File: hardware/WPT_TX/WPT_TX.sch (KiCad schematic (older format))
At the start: 121 parts, among them J1 Conn_01x01, J10 Conn_01x01, J2 Conn_01x01, J3 Conn_Coaxial, J4 Conn_Coaxial, J5 Conn_Coaxial, J6 Conn_02x05_Odd_Even, J7 Conn_01x03, J8 Conn_01x04, J9 Conn_01x01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

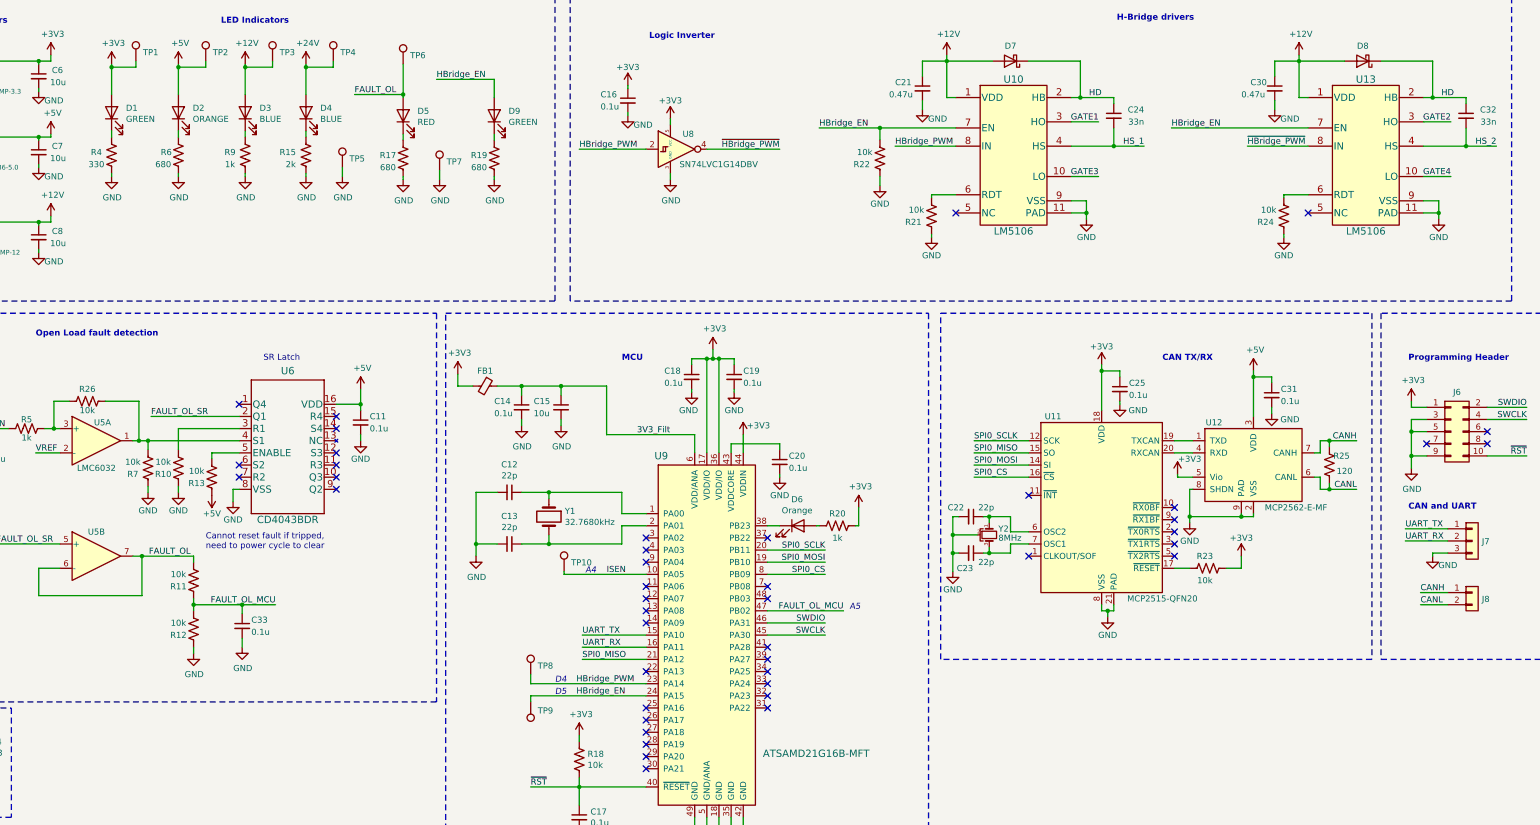
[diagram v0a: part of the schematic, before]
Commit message: Schematic Updates
- Removed "HD" net label from HB pins on gate drivers. This resulted in a critical failure on the original board and was fixed with a bodge.
- Added an extra voltage divider to ISEN input to reduce chance of 5V overvolt scenario.
- Increased series resistor value for blue LEDs by a factor of 2. Waaaay too bright.
- Decreased series resistor for 3V3 LED indicator, too dim.
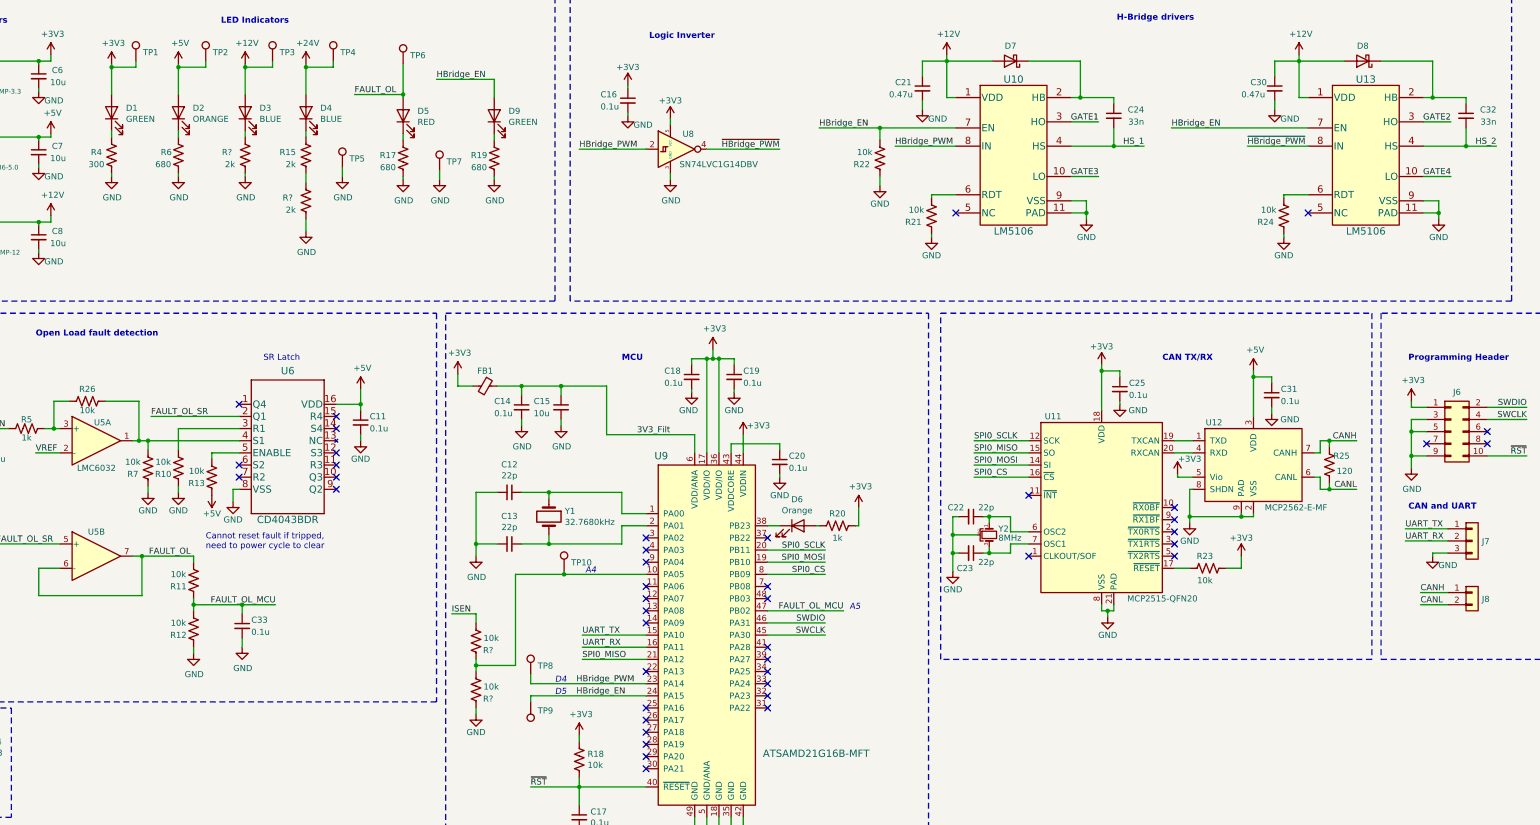
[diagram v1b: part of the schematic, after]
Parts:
- removed R9: 1k, Resistor_SMD:R_0603_1608Metric, symbol WPT_TX-rescue:R_US-Device
- added R? (x2): 10k, Resistor_SMD:R_0603_1608Metric, symbol WPT_TX-rescue:R_US-Device
- added R? (x2): 2k, Resistor_SMD:R_0603_1608Metric, symbol WPT_TX-rescue:R_US-Device
- R4: value 330 -> 300; Digikey RHM330DCT-ND -> P300BZCT-ND
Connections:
- net GND: now also R?.1, R?.1, R?.1; no longer R15.1
- net HD: no longer C24.1, C32.1, D7.1 (K), D8.1 (K), U10.2 (HB), U13.2 (HB)
- net ISEN: now also R?.2; no longer TP10.1, U9.10 (PA05)
- net at D3.1 (K): now also R?.2
- new net: C32.1, D8.1 (K), U13.2 (HB)
- new net: R?.1, R?.2, TP10.1, U9.10 (PA05)
- new net: R15.1, R?.2
- new net: C24.1, D7.1 (K), U10.2 (HB)
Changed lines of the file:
@@
 Sheet 1 1
 Title "Wireless Charger TX Board"
-Date "2020-11-08"
-Rev "001"
-Comp "AUV Capstone"
+Date "2021-05-24"
+Rev "v1.1"
+Comp "AUV Capstone Project"
 Comment1 "Mark Belbin"
 Comment2 ""
@@
 Text Label 2750 6700 2    50   ~ 0
 ISEN
-Text Label 7700 7900 0    50   ~ 0
-ISEN
 $Comp
 L WPT_TX-rescue:LMC6082-Amplifier_Operational U5
@@
 P 3625 4450
 F 0 "R4" H 3750 4425 50  0000 C CNN
-F 1 "330" H 3750 4525 50  0000 C CNN
+F 1 "300" H 3750 4525 50  0000 C CNN
 F 2 "Resistor_SMD:R_0603_1608Metric" V 3665 4440 50  0001 C CNN
 F 3 "~" H 3625 4450 50  0001 C CNN
-F 4 "RHM330DCT-ND" H 3625 4450 50  0001 C CNN "Digikey"
+F 4 "P300BZCT-ND" H 3625 4450 50  0001 C CNN "Digikey"
 	1    3625 4450
 	-1   0    0    1
@@
 Wire Wire Line
 	5225 4300 5225 4250
-Wire Wire Line
-	5225 4600 5225 4625
 $Comp
 L WPT_TX-rescue:GND-power #PWR040
 U 1 1 60543B6B
-P 5225 4625
-F 0 "#PWR040" H 5225 4375 50  0001 C CNN
-F 1 "GND" H 5230 4452 50  0000 C CNN
-F 2 "" H 5225 4625 50  0001 C CNN
-F 3 "" H 5225 4625 50  0001 C CNN
-	1    5225 4625
+P 5225 5075
+F 0 "#PWR040" H 5225 4825 50  0001 C CNN
+F 1 "GND" H 5230 4902 50  0000 C CNN
+F 2 "" H 5225 5075 50  0001 C CNN
+F 3 "" H 5225 5075 50  0001 C CNN
+	1    5225 5075
 	1    0    0    -1
 $EndComp
@@
 Wire Wire Line
 	5675 6750 5675 6800
-Wire Wire Line
-	4175 6700 4175 6875
-$Comp
-L WPT_TX-rescue:GND-power #PWR034
-U 1 1 60930002
-P 4175 7225
-F 0 "#PWR034" H 4175 6975 50  0001 C CNN
-F 1 "GND" H 4175 7075 50  0000 C CNN
-F 2 "" H 4175 7225 50  0001 C CNN
-F 3 "" H 4175 7225 50  0001 C CNN
-	1    4175 7225
-	1    0    0    -1
-$EndComp
-$Comp
-L WPT_TX-rescue:R_US-Device R10
-U 1 1 60931174
-P 4175 7025
-F 0 "R10" H 4300 7075 50  0000 C CNN
-F 1 "10k" H 4300 6975 50  0000 C CNN
-F 2 "Resistor_SMD:R_0603_1608Metric" V 4215 7015 50  0001 C CNN
-F 3 "~" H 4175 7025 50  0001 C CNN
-F 4 "RHM10KDCT-ND" H 4175 7025 50  0001 C CNN "Digikey"
-	1    4175 7025
-	-1   0    0    1
-$EndComp
-Wire Wire Line
-	4175 7175 4175 7225
 $Comp
 L WPT_TX-rescue:R_US-Device R16
@@
 Text Label 8025 1175 0    50   ~ 0
 HD
-Text Label 11775 3975 2    50   ~ 0
-HD
 Wire Wire Line
 	11525 4375 11875 4375
@@
 	1    0    0    -1
 $EndComp
-$Comp
-L WPT_TX-rescue:R_US-Device R9
-U 1 1 616EAE40
-P 4725 4450
-F 0 "R9" H 4850 4425 50  0000 C CNN
-F 1 "1k" H 4850 4525 50  0000 C CNN
-F 2 "Resistor_SMD:R_0603_1608Metric" V 4765 4440 50  0001 C CNN
-F 3 "~" H 4725 4450 50  0001 C CNN
-F 4 "RHM1.0KDCT-ND" H 4725 4450 50  0001 C CNN "Digikey"
-	1    4725 4450
-	-1   0    0    1
-$EndComp
 Wire Wire Line
 	4950 3675 4950 3725
@@
 	1    0    0    -1
 $EndComp
-Text Label 14675 3975 2    50   ~ 0
-HD
 Wire Wire Line
 	14425 4375 14775 4375
@@
 Wire Notes Line
 	1050 9900 1050 9000
+Wire Wire Line
+	4175 6700 4175 6875
+$Comp
+L WPT_TX-rescue:R_US-Device R10
+U 1 1 60931174
+P 4175 7025
+F 0 "R10" H 4300 7075 50  0000 C CNN
+F 1 "10k" H 4300 6975 50  0000 C CNN
+F 2 "Resistor_SMD:R_0603_1608Metric" V 4215 7015 50  0001 C CNN
+F 3 "~" H 4175 7025 50  0001 C CNN
+F 4 "RHM10KDCT-ND" H 4175 7025 50  0001 C CNN "Digikey"
+	1    4175 7025
+	-1   0    0    1
+$EndComp
+Wire Wire Line
+	4175 7175 4175 7225
+$Comp
+L WPT_TX-rescue:GND-power #PWR034
+U 1 1 60930002
+P 4175 7225
+F 0 "#PWR034" H 4175 6975 50  0001 C CNN
+F 1 "GND" H 4175 7075 50  0000 C CNN
+F 2 "" H 4175 7225 50  0001 C CNN
+F 3 "" H 4175 7225 50  0001 C CNN
+	1    4175 7225
+	1    0    0    -1
+$EndComp
+Wire Wire Line
+	6625 8300 6625 8225
+Wire Wire Line
+	6625 8700 6625 8650
+Wire Wire Line
+	6625 9000 6625 9050
+$Comp
+L WPT_TX-rescue:GND-power #PWR?
+U 1 1 60B7C0DE
+P 6625 9050
+F 0 "#PWR?" H 6625 8800 50  0001 C CNN
+F 1 "GND" H 6625 8900 50  0000 C CNN
+F 2 "" H 6625 9050 50  0001 C CNN
+F 3 "" H 6625 9050 50  0001 C CNN
+	1    6625 9050
+	1    0    0    -1
+$EndComp
+$Comp
+L WPT_TX-rescue:R_US-Device R?
+U 1 1 60B7C0ED
+P 6625 8450
+F 0 "R?" H 6525 8525 50  0000 C CNN
+F 1 "10k" H 6500 8425 50  0000 C CNN
+F 2 "Resistor_SMD:R_0603_1608Metric" V 6665 8440 50  0001 C CNN
+F 3 "~" H 6625 8450 50  0001 C CNN
+F 4 "RHM10KDCT-ND" H 6625 8450 50  0001 C CNN "Digikey"
+	1    6625 8450
+	-1   0    0    1
+$EndComp
+Connection ~ 6625 8650
+Wire Wire Line
+	6625 8650 6625 8600
+Wire Wire Line
+	6950 8650 6950 7900
+Wire Wire Line
+	6950 7900 7350 7900
+Wire Wire Line
+	6625 8650 6950 8650
+Connection ~ 7350 7900
+Wire Wire Line
+	6625 8225 6425 8225
+$Comp
+L WPT_TX-rescue:R_US-Device R?
+U 1 1 60C2E8D1
+P 6625 8850
+F 0 "R?" H 6525 8925 50  0000 C CNN
+F 1 "10k" H 6500 8825 50  0000 C CNN
+F 2 "Resistor_SMD:R_0603_1608Metric" V 6665 8840 50  0001 C CNN
+F 3 "~" H 6625 8850 50  0001 C CNN
+F 4 "RHM10KDCT-ND" H 6625 8850 50  0001 C CNN "Digikey"
+	1    6625 8850
+	-1   0    0    1
+$EndComp
+Text Label 6425 8225 0    50   ~ 0
+ISEN
+$Comp
+L WPT_TX-rescue:R_US-Device R?
+U 1 1 60C6C779
+P 4725 4450
+F 0 "R?" H 4875 4425 50  0000 C CNN
+F 1 "2k" H 4850 4525 50  0000 C CNN
+F 2 "Resistor_SMD:R_0603_1608Metric" V 4765 4440 50  0001 C CNN
+F 3 "~" H 4725 4450 50  0001 C CNN
+F 4 "541-2790-1-ND" H 4725 4450 50  0001 C CNN "Digikey"
+	1    4725 4450
+	-1   0    0    1
+$EndComp
+$Comp
+L WPT_TX-rescue:R_US-Device R?
+U 1 1 60CA7F5A
+P 5225 4825
+F 0 "R?" H 5375 4800 50  0000 C CNN
+F 1 "2k" H 5350 4900 50  0000 C CNN
+F 2 "Resistor_SMD:R_0603_1608Metric" V 5265 4815 50  0001 C CNN
+F 3 "~" H 5225 4825 50  0001 C CNN
+F 4 "541-2790-1-ND" H 5225 4825 50  0001 C CNN "Digikey"
+	1    5225 4825
+	-1   0    0    1
+$EndComp
+Wire Wire Line
+	5225 4600 5225 4675
+Wire Wire Line
+	5225 5075 5225 4975
 $EndSCHEMATC

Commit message: Updated PCB
- Added four extra resistors from schematic changes to PCB.
- Removed HD connections in gate driver layout.
- Regenerated gerbers
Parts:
- gave numbers to parts that had none: 4
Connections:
- net ISEN: now also TP10.1
- net at R28.1, R29.2, U9.10 (PA05): no longer TP10.1
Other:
- moved on the sheet: TP10
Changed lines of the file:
@@
 Wire Wire Line
 	9025 8200 9650 8200
-Wire Wire Line
-	7350 7875 7350 7900
-Wire Wire Line
-	7350 7900 8025 7900
 $Comp
 L WPT_TX-rescue:TestPoint-Connector TP2
@@
 L WPT_TX-rescue:TestPoint-Connector TP10
 U 1 1 6286B951
-P 7350 7875
-F 0 "TP10" H 7408 7947 50  0000 L CNN
-F 1 "TestPoint" H 7408 7902 50  0001 L CNN
-F 2 "TestPoint:TestPoint_Loop_D1.80mm_Drill1.0mm_Beaded" H 7550 7875 50  0001 C CNN
-F 3 "~" H 7550 7875 50  0001 C CNN
-F 4 "36-5117-ND" H 7350 7875 50  0001 C CNN "Digikey"
-	1    7350 7875
+P 2775 6500
+F 0 "TP10" H 2833 6572 50  0000 L CNN
+F 1 "TestPoint" H 2833 6527 50  0001 L CNN
+F 2 "TestPoint:TestPoint_Loop_D1.80mm_Drill1.0mm_Beaded" H 2975 6500 50  0001 C CNN
+F 3 "~" H 2975 6500 50  0001 C CNN
+F 4 "36-5117-ND" H 2775 6500 50  0001 C CNN "Digikey"
+	1    2775 6500
 	1    0    0    -1
 $EndComp
@@
 	6625 9000 6625 9050
 $Comp
-L WPT_TX-rescue:GND-power #PWR?
+L WPT_TX-rescue:GND-power #PWR0103
 U 1 1 60B7C0DE
 P 6625 9050
-F 0 "#PWR?" H 6625 8800 50  0001 C CNN
+F 0 "#PWR0103" H 6625 8800 50  0001 C CNN
 F 1 "GND" H 6625 8900 50  0000 C CNN
 F 2 "" H 6625 9050 50  0001 C CNN
@@
 $EndComp
 $Comp
-L WPT_TX-rescue:R_US-Device R?
+L WPT_TX-rescue:R_US-Device R28
 U 1 1 60B7C0ED
 P 6625 8450
-F 0 "R?" H 6525 8525 50  0000 C CNN
+F 0 "R28" H 6500 8525 50  0000 C CNN
 F 1 "10k" H 6500 8425 50  0000 C CNN
 F 2 "Resistor_SMD:R_0603_1608Metric" V 6665 8440 50  0001 C CNN
@@
 	6950 8650 6950 7900
 Wire Wire Line
-	6950 7900 7350 7900
-Wire Wire Line
 	6625 8650 6950 8650
-Connection ~ 7350 7900
 Wire Wire Line
 	6625 8225 6425 8225
 $Comp
-L WPT_TX-rescue:R_US-Device R?
+L WPT_TX-rescue:R_US-Device R29
 U 1 1 60C2E8D1
 P 6625 8850
-F 0 "R?" H 6525 8925 50  0000 C CNN
+F 0 "R29" H 6500 8925 50  0000 C CNN
 F 1 "10k" H 6500 8825 50  0000 C CNN
 F 2 "Resistor_SMD:R_0603_1608Metric" V 6665 8840 50  0001 C CNN
@@
 ISEN
 $Comp
-L WPT_TX-rescue:R_US-Device R?
+L WPT_TX-rescue:R_US-Device R9
 U 1 1 60C6C779
 P 4725 4450
-F 0 "R?" H 4875 4425 50  0000 C CNN
+F 0 "R9" H 4875 4425 50  0000 C CNN
 F 1 "2k" H 4850 4525 50  0000 C CNN
 F 2 "Resistor_SMD:R_0603_1608Metric" V 4765 4440 50  0001 C CNN
@@
 $EndComp
 $Comp
-L WPT_TX-rescue:R_US-Device R?
+L WPT_TX-rescue:R_US-Device R27
 U 1 1 60CA7F5A
 P 5225 4825
-F 0 "R?" H 5375 4800 50  0000 C CNN
+F 0 "R27" H 5375 4800 50  0000 C CNN
 F 1 "2k" H 5350 4900 50  0000 C CNN
 F 2 "Resistor_SMD:R_0603_1608Metric" V 5265 4815 50  0001 C CNN
@@
 Wire Wire Line
 	5225 5075 5225 4975
+Wire Wire Line
+	2775 6500 2775 6700
+Connection ~ 2775 6700
+Wire Wire Line
+	6950 7900 8025 7900
 $EndSCHEMATC
